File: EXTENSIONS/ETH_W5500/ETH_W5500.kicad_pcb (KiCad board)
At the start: 2 copper layers, 59.5 x 34.3 mm, 69 parts, among them J1 EXT, J2 WE-634008137521, J3 MM-690367290876, U2 AP1117-33, U3 W5500, Y1 25M

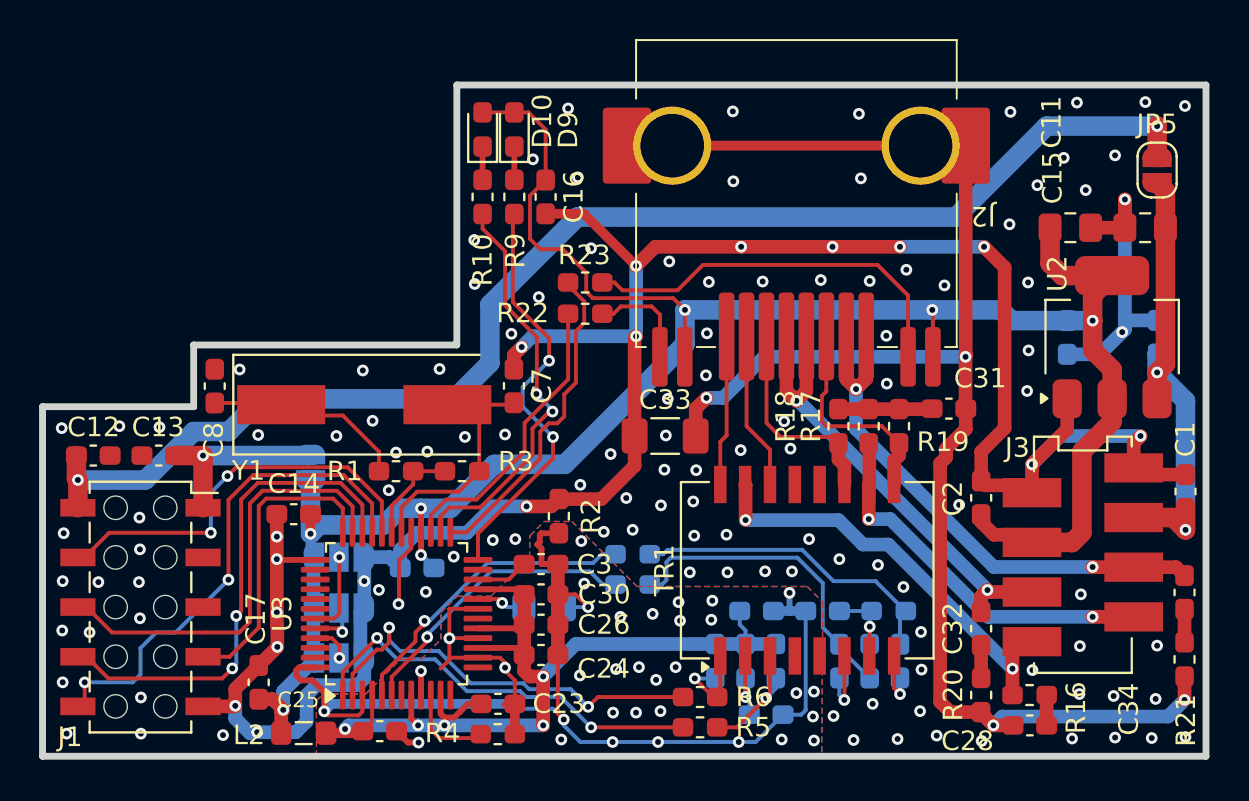
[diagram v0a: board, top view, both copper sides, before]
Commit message: Improve documentation and ETH-Extension
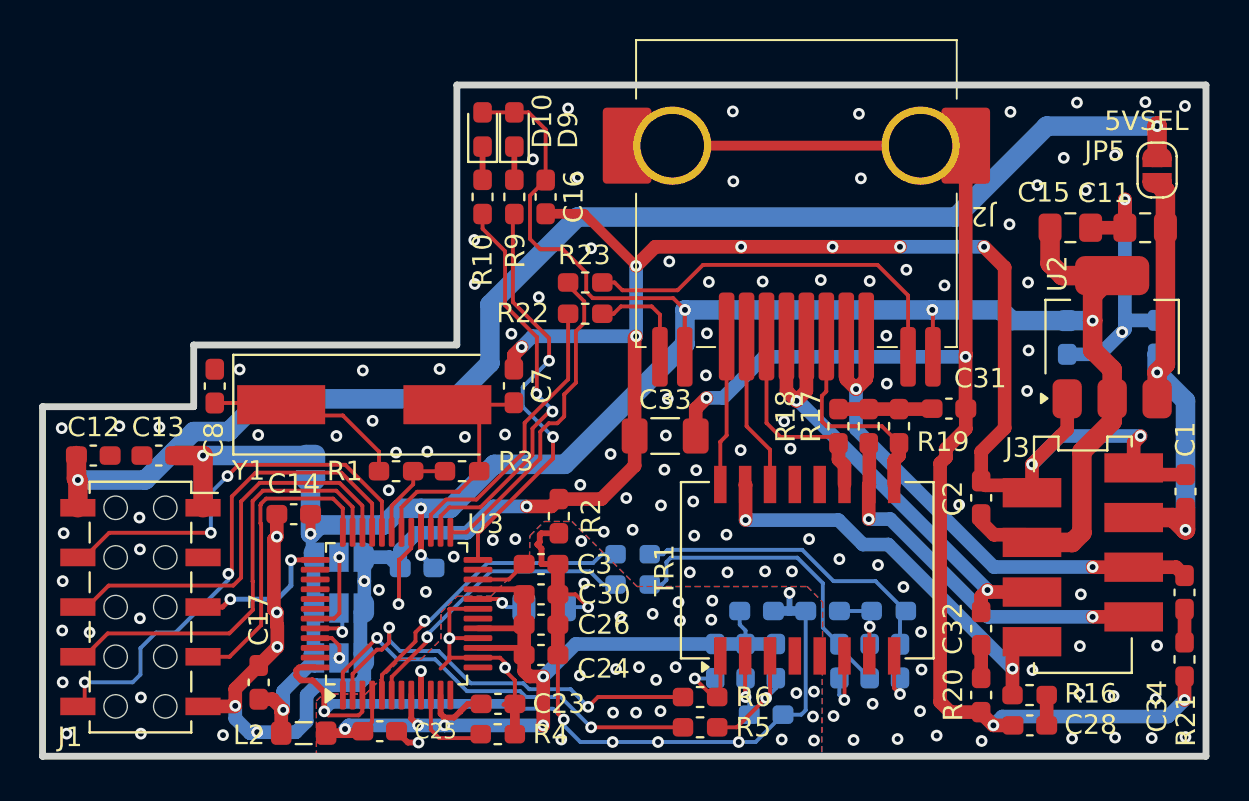
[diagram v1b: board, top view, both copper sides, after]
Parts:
- TR1: footprint the78mole:Transformer_Ethernet_Wuerth_749013011A -> Transformer_SMD:Transformer_Ethernet_Wuerth_749013011A
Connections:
- U3 pad 34: MOSI -> MISO
- U3 pad 35: MISO -> MOSI
- U3 pad 37: GND -> SDA_X
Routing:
- net SDA_X: track 0.00 -> 7.50 mm, vias 0 -> 2
- net MOSI: track 25.8 -> 22.5 mm, vias 2 -> 0
- net GND: track 139.5 -> 137.7 mm, vias 133 -> 130
- net MISO: track 22.8 -> 21.3 mm
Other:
- board text added: "3V3SEL"
- board text added: "5VSEL"
- board text added: "PMODE"
